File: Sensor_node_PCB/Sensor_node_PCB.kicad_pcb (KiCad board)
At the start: 2 copper layers, 100 x 95 mm, 37 parts, among them J1 DIP28_socket, J2 Logic power, J3 Programmer, J4 SPI breakout, Q1 NMOS, Q2 NMOS, Q3 NMOS, U1 INA219AxD

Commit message: PCB corrections and improvements
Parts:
- Q1, Q2, Q3: footprint Package_TO_SOT_THT:TO-220-3_Vertical -> Package_TO_SOT_THT:TO-220F-3_Horizontal_TabUp
- R1: footprint Resistor_THT:R_Axial_DIN0309_L9.0mm_D3.2mm_P12.70mm_Horizontal -> Capacitor_SMD:C_1206_3216Metric_Pad1.33x1.80mm_HandSolder
- moved Q2 29.0 mm to (217.4, 134.4), turned to 180 degrees
- moved R3 13.7 mm to (204.6, 52.7)
- moved R4 10.5 mm to (216.7, 52.6)
- moved R12 8.05 mm to (169.9, 136.4), turned to 180 degrees
- moved Q3 6.55 mm to (186.7, 138.7), turned to 90 degrees
- moved R14 6.36 mm to (130.4, 76.0)
- moved R5 6.36 mm to (141.4, 63.4)
- moved R6 6.36 mm to (146.7, 63.4)
- moved R13 6.36 mm to (135.8, 63.4)
- moved Q1 5.63 mm to (188.6, 119.5), turned to 90 degrees
- moved J2 4.91 mm to (130.6, 99.0)
- moved J3 4.53 mm to (130.8, 92.2)
- moved R1 4.20 mm to (160.2, 52.7)
- moved C5 2.65 mm to (158.1, 101.5)
- moved C3 2.38 mm to (158.0, 128.6)
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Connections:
- J4 pad 1: MOSI -> CLK
- J4 pad 2: CLK -> MISO
- J4 pad 3: MISO -> MOSI
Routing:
- net Net-(Q3-D): track 0.00 -> 68.6 mm
- net Net-(Q2-G): track 12.5 -> 64.0 mm
- net Net-(Q2-D): track 0.00 -> 30.1 mm
- net Net-(Q3-G): track 15.7 -> 42.9 mm
- net Net-(Q1-D): track 0.00 -> 21.7 mm
- net Net-(Q1-G): track 19.7 -> 30.2 mm
- net MOSI: track 37.7 -> 46.1 mm
- net SDA: track 63.6 -> 67.8 mm
- net PWM3: track 9.01 -> 12.8 mm
- net VDD: track 97.2 -> 94.0 mm
- net PGD2: track 119.4 -> 116.6 mm
- net LED1: track 43.4 -> 40.8 mm
- net SCL: track 57.7 -> 60.2 mm
- net LED2: track 38.1 -> 35.7 mm
- net PWM2: track 9.08 -> 11.3 mm
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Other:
- outline, holes or cut-outs redrawn

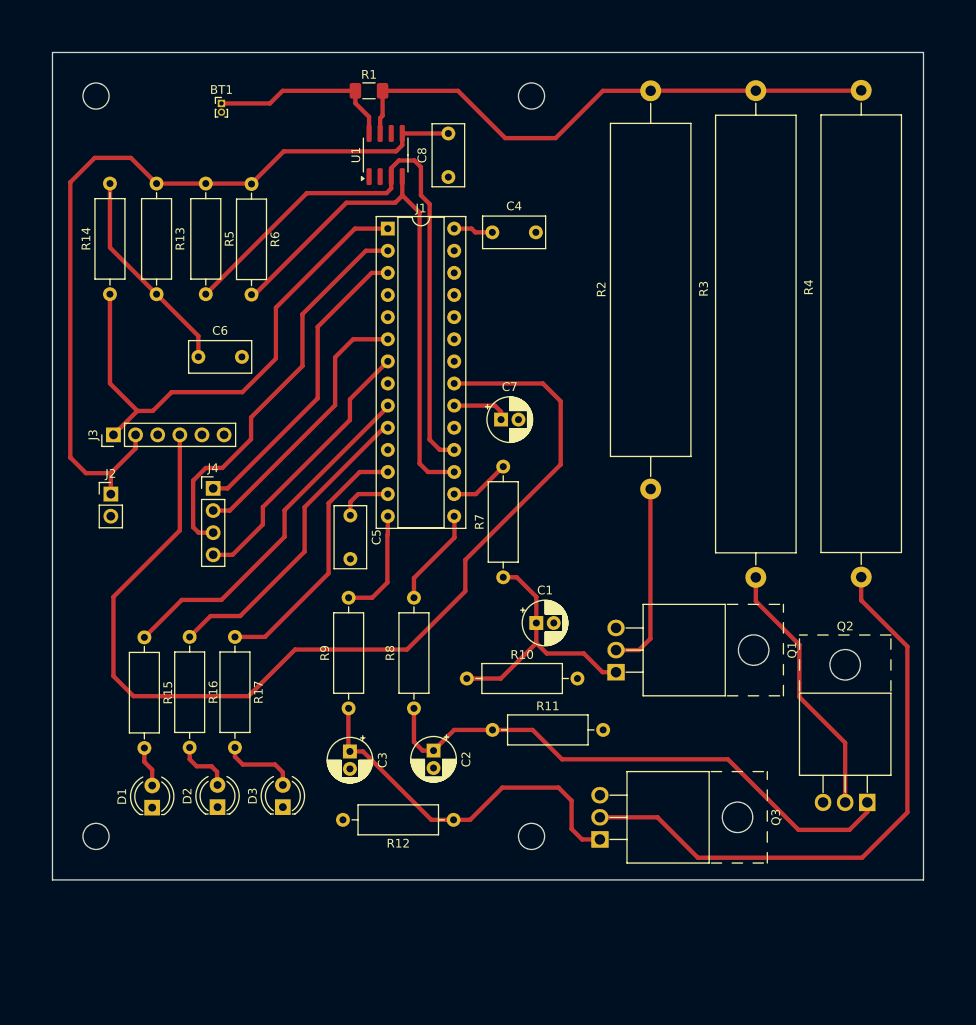
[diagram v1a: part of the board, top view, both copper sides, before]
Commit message: PCB layout redone as shield for devboard
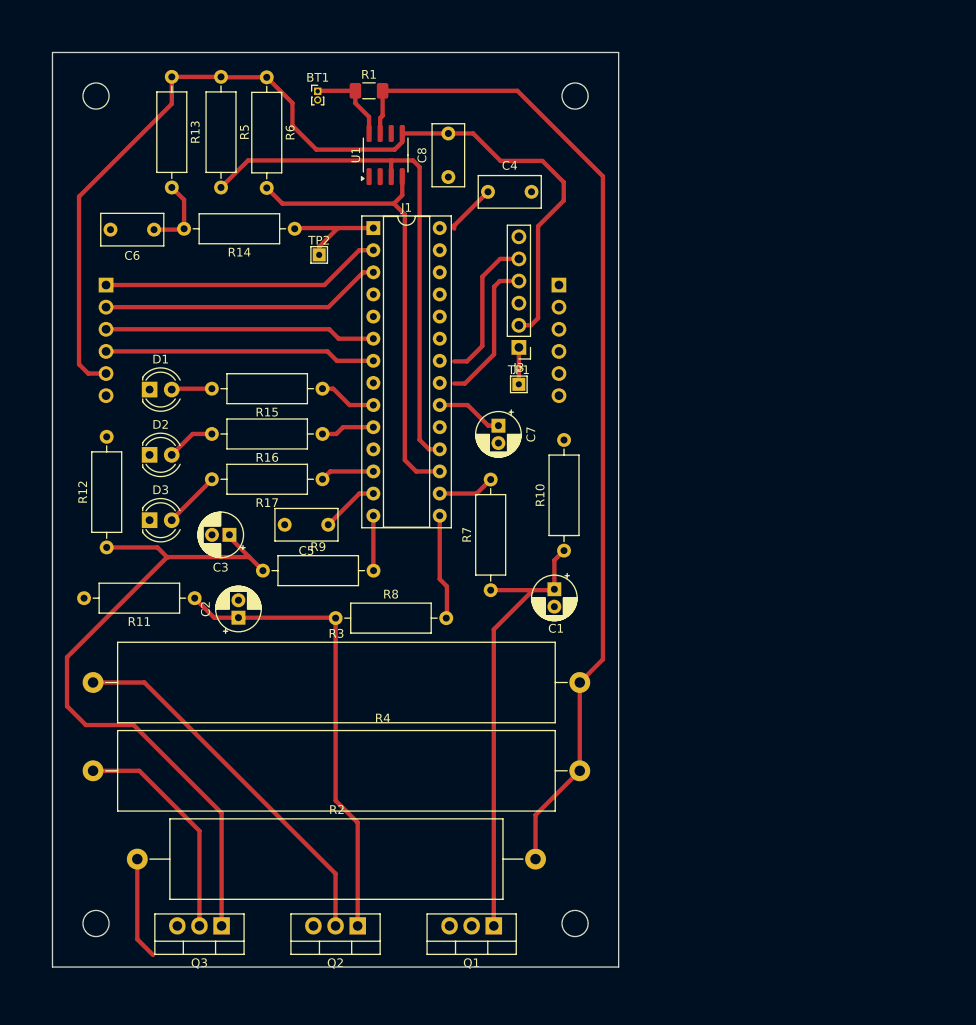
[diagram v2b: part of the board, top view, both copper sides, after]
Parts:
- added TP1: TestPoint, TestPoint:TestPoint_THTPad_1.5x1.5mm_Drill0.7mm, F.Cu at (177.4, 86.4)
- added TP2: TestPoint, TestPoint:TestPoint_THTPad_1.5x1.5mm_Drill0.7mm, F.Cu at (154.5, 71.5)
- J2: value Logic power -> Dummy header; footprint Connector_PinHeader_2.54mm:PinHeader_1x02_P2.54mm_Vertical -> Connector_PinHeader_2.54mm:PinHeader_1x06_P2.54mm_Vertical; moved to B.Cu
- J4: footprint Connector_PinHeader_2.54mm:PinHeader_1x04_P2.54mm_Vertical -> Connector_PinHeader_2.54mm:PinHeader_1x06_P2.54mm_Vertical; moved to B.Cu
- Q1, Q2, Q3: footprint Package_TO_SOT_THT:TO-220F-3_Horizontal_TabUp -> Package_TO_SOT_THT:TO-220-3_Vertical
- moved R2 89.2 mm to (179.3, 140.9), turned to 180 degrees
- moved R4 84.5 mm to (184.4, 130.8), turned to 180 degrees
- moved R3 70.9 mm to (184.4, 120.6), turned to 180 degrees
- moved Q2 60.2 mm to (158.9, 148.6)
- moved J2 56.8 mm to (182.0, 75.0), turned to 180 degrees
- moved R12 50.6 mm to (130.1, 105.1), turned to 90 degrees
- moved D1 48.0 mm to (135.0, 87.0), turned to 0 degrees
- moved J3 47.6 mm to (177.4, 82.2), turned to 180 degrees
- moved Q3 44.6 mm to (143.3, 148.6), turned to 180 degrees
- moved D2 41.2 mm to (135.0, 94.5), turned to 0 degrees
- moved R11 37.4 mm to (140.2, 111.0), turned to 180 degrees
- moved D3 36.3 mm to (135.0, 102.0), turned to 0 degrees
- moved R15 35.1 mm to (154.8, 86.9), turned to 180 degrees
- moved Q1 32.3 mm to (174.5, 148.6), turned to 180 degrees
- moved C3 28.5 mm to (144.2, 103.7), turned to 180 degrees
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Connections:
- J1 pad 2: MOSI -> CS
- J1 pad 7: CS -> MOSI
- J2 pad 1: VDD -> unconnected-(J2-Pin_1-Pad1)
- J2 pad 2: GND -> unconnected-(J2-Pin_2-Pad2)
- J4 pad 1: CLK -> CS
- J4 pad 2: MISO -> CLK
- J4 pad 3: MOSI -> MISO
- J4 pad 4: CS -> MOSI
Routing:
- net PGD2: track 116.6 -> 16.8 mm
- net Net-(U1-IN-): track 64.5 -> 116.0 mm
- net Net-(Q3-D): track 68.6 -> 26.0 mm
- net MCLR: track 59.4 -> 17.3 mm
- net Net-(Q3-G): track 42.9 -> 80.2 mm
- net LED1: track 40.8 -> 6.62 mm
- net LED2: track 35.7 -> 6.16 mm
- net LED3: track 30.1 -> 6.21 mm
- net Net-(Q1-G): track 30.2 -> 52.7 mm
- net VDD: track 94.0 -> 114.0 mm
- net PGC2: track 0.00 -> 17.0 mm
- net Net-(C6-Pad1): track 24.1 -> 8.82 mm
- net MOSI: track 46.1 -> 31.1 mm
- net Net-(Q2-D): track 30.1 -> 42.9 mm
- net Net-(BT1-+): track 21.5 -> 9.90 mm
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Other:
- board size 100 x 95 mm -> 65 x 105 mm

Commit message: PCB redone according to fabrication specs
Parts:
- added TP3: TestPoint, TestPoint:TestPoint_THTPad_1.5x1.5mm_Drill0.7mm, B.Cu at (168.7, 69.7)
- added TP4: TestPoint, TestPoint:TestPoint_THTPad_1.5x1.5mm_Drill0.7mm, B.Cu at (146.9, 51.0)
- BT1: footprint Connector_PinHeader_1.00mm:PinHeader_1x02_P1.00mm_Vertical -> Connector_PinHeader_2.00mm:PinHeader_1x02_P2.00mm_Vertical
- C4, C5, C6, C8, R1, R10, R11, R12, R13, R14, R15, R16, R17, R2, R3, R4, R5, R6, R7, R8, R9, TP1, TP2, U1: moved to B.Cu
- moved R12 44.5 mm to (174.6, 107.1), turned to 0 degrees
- moved TP1 36.8 mm to (146.9, 65.8), turned to 180 degrees
- moved Q1 36.4 mm to (138.1, 148.9), turned to 0 degrees
- moved R11 35.4 mm to (174.6, 102.3), turned to 0 degrees
- moved R6 29.0 mm to (126.9, 70.5), turned to 0 degrees
- moved C2 26.5 mm to (169.9, 103.6)
- moved Q3 26.1 mm to (169.4, 148.9), turned to 0 degrees
- moved D1 25.9 mm to (127.5, 111.8), turned to 90 degrees
- moved C3 25.4 mm to (168.8, 109.5), turned to 0 degrees
- moved C1 23.2 mm to (175.1, 87.6), turned to 180 degrees
- moved R5 22.3 mm to (126.9, 66.3), turned to 0 degrees
- moved C8 22.1 mm to (151.2, 49.9), turned to -90 degrees
- moved D2 18.1 mm to (140.2, 111.8), turned to 90 degrees
- moved R7 18.0 mm to (178.2, 92.5), turned to 180 degrees
- moved R9 17.3 mm to (165.2, 109.5), turned to 180 degrees
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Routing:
- net VDD: track 114.0 -> 64.2 mm
- net Net-(Q3-D): track 26.0 -> 63.2 mm
- net Net-(Q1-G): track 52.7 -> 83.7 mm
- net Net-(Q3-G): track 80.2 -> 51.9 mm
- net Net-(Q2-D): track 42.9 -> 55.2 mm
- net Net-(D1-A): track 4.65 -> 15.4 mm
- net LED2: track 6.16 -> 16.7 mm
- net Net-(D2-A): track 5.65 -> 16.0 mm
- net LED3: track 6.21 -> 16.2 mm
- net LED1: track 6.62 -> 15.7 mm
- net MOSI: track 31.1 -> 22.5 mm
- net MISO: track 31.1 -> 22.5 mm
- net PGD2: track 16.8 -> 25.0 mm
- net CLK: track 32.3 -> 24.6 mm
- net CS: track 32.3 -> 24.6 mm
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- added copper zone on B.Cu, net GND
- removed copper zone on F.Cu, net GND
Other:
- board text added: "PROG"
- board text added: "SPI"
